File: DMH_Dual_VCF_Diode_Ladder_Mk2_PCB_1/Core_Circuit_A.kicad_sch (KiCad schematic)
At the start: 41 parts, among them SW1 SW_SPDT, SW2 SW_SPDT, SW3 SW_SPDT, U3 TL074, U5 TL074

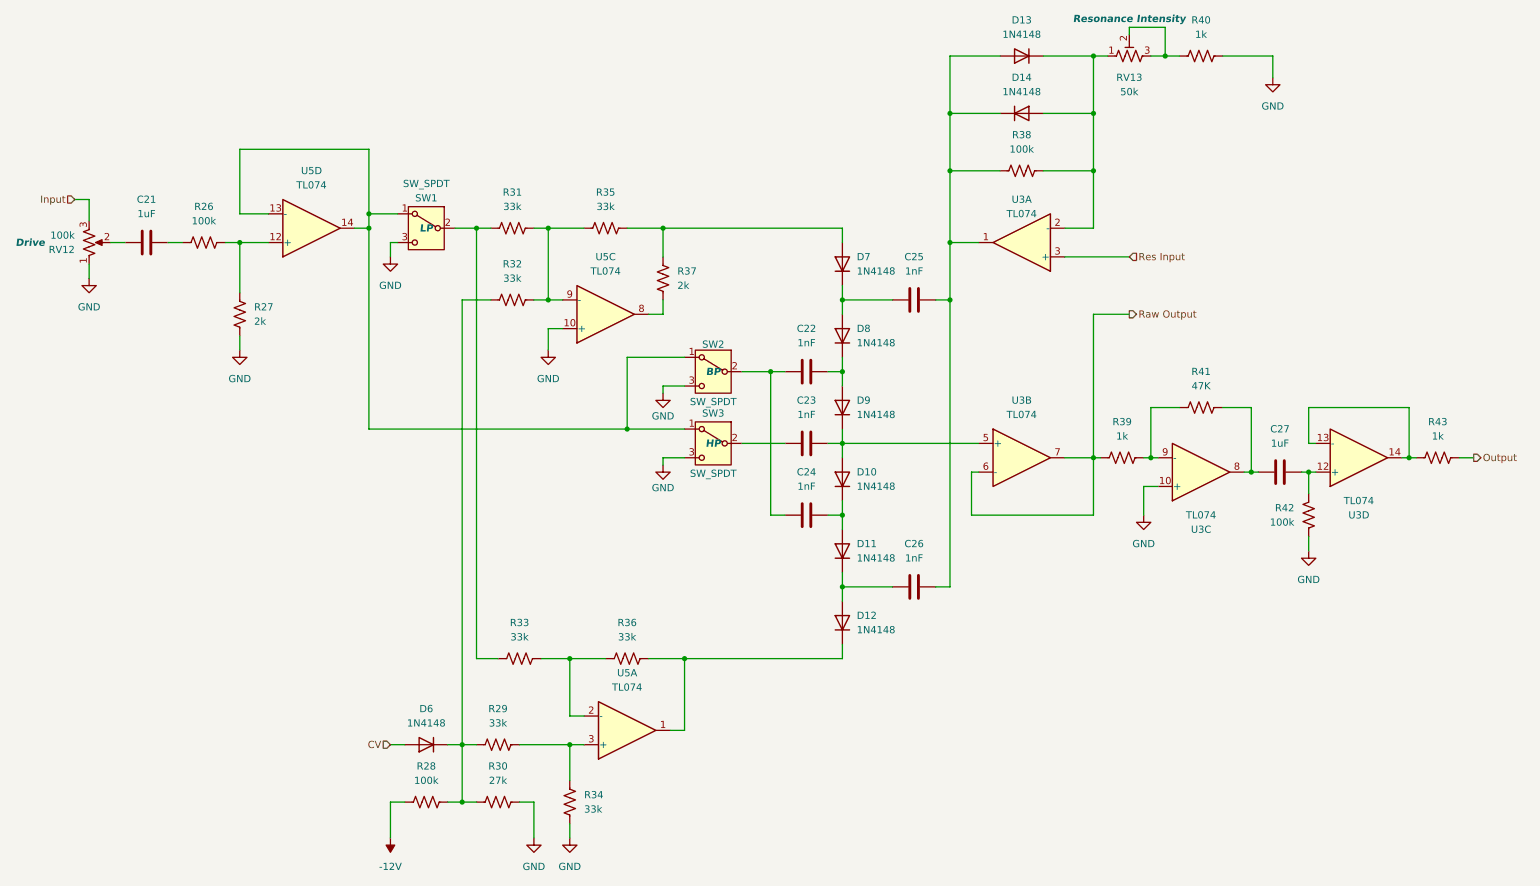
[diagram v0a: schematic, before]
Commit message: Added board-to-board pins to schematic
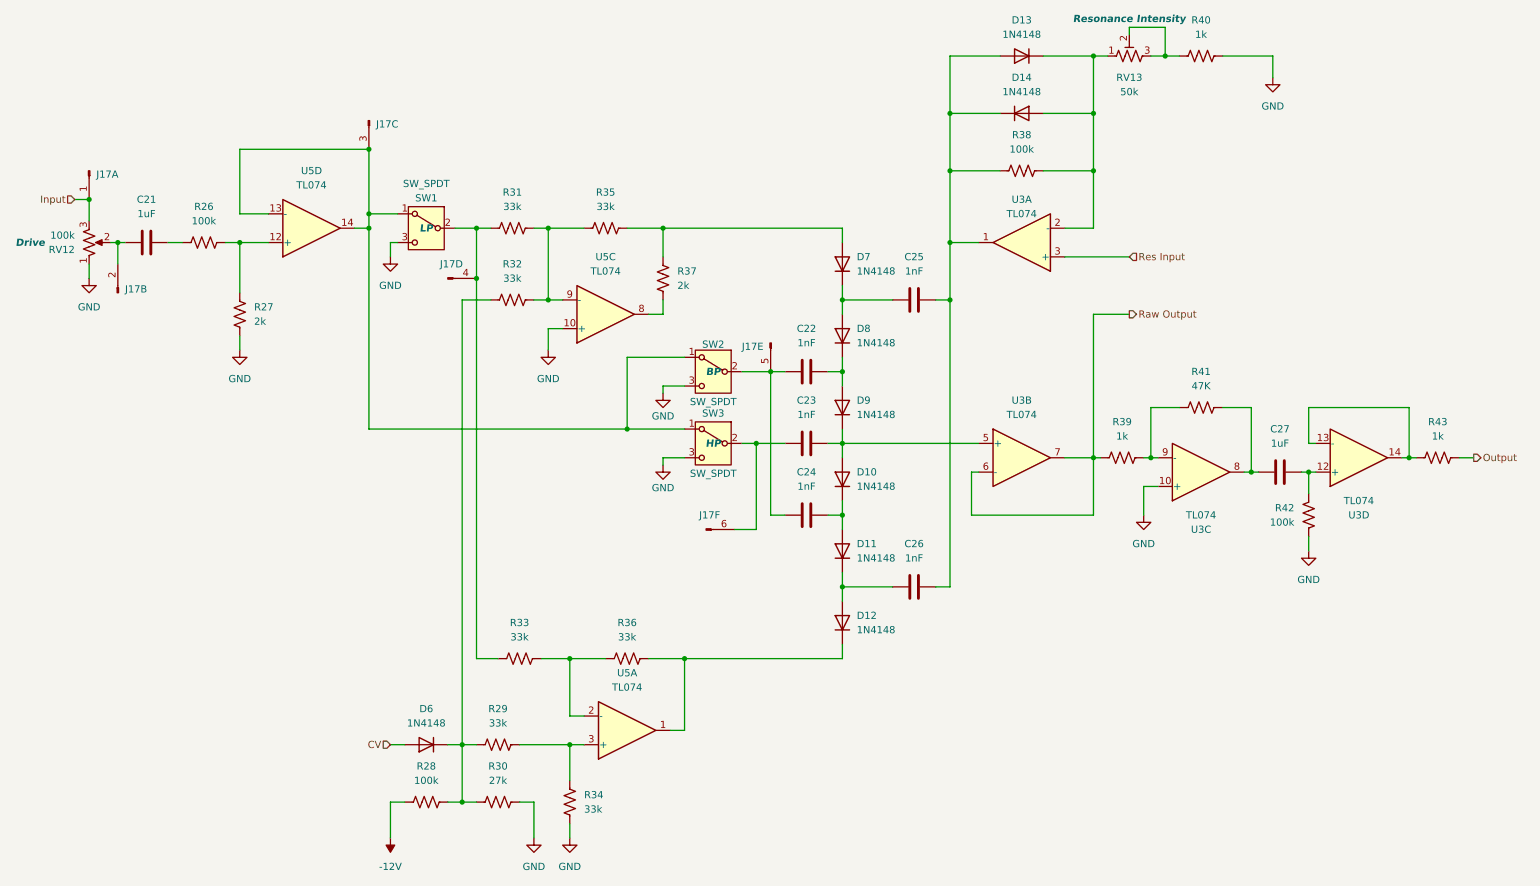
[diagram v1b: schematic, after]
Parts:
- added J17: Conn_01x10_PinHeader, Connector_PinHeader_2.54mm:PinHeader_1x10_P2.54mm_Vertical, symbol SynthStuff:Conn_01x10_PinHeader
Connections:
- net Input: now also J17.1 (Pin_1)
- net at C21.1, RV12.2: now also J17.2 (Pin_2)
- net at C22.1, C24.1, SW2.2 (B): now also J17.5 (Pin_5)
- net at SW1.1 (A), SW2.1 (A), SW3.1 (A)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: now also J17.3 (Pin_3)
- net at R31.1, R33.1, SW1.2 (B): now also J17.4 (Pin_4)
- net at C23.1, SW3.2 (B): now also J17.6 (Pin_6)

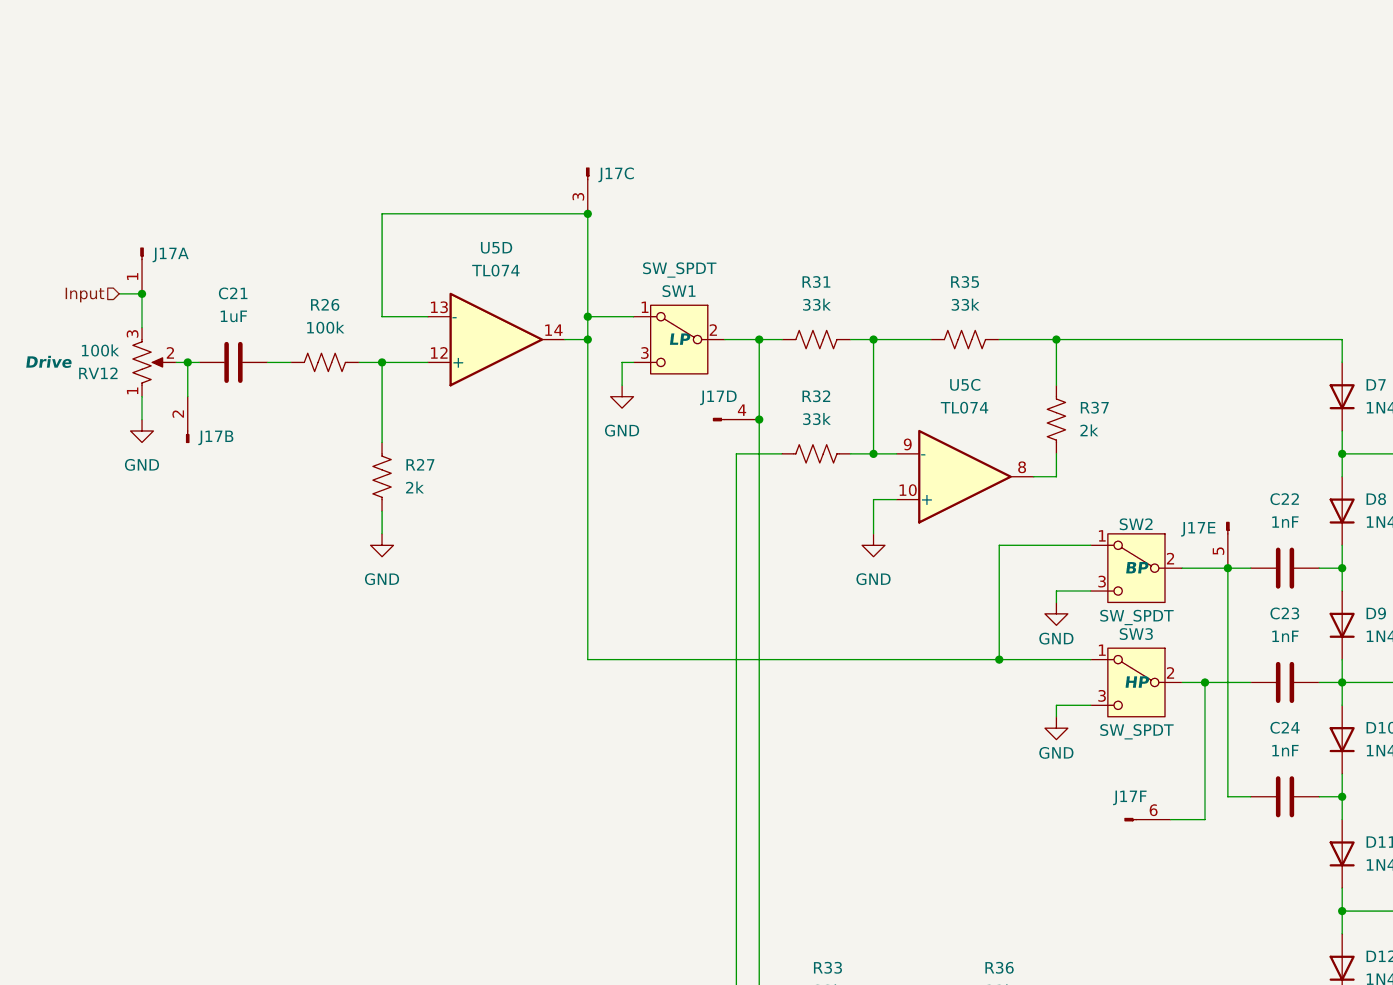
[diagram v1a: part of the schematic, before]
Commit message: Created Drive CV circuits
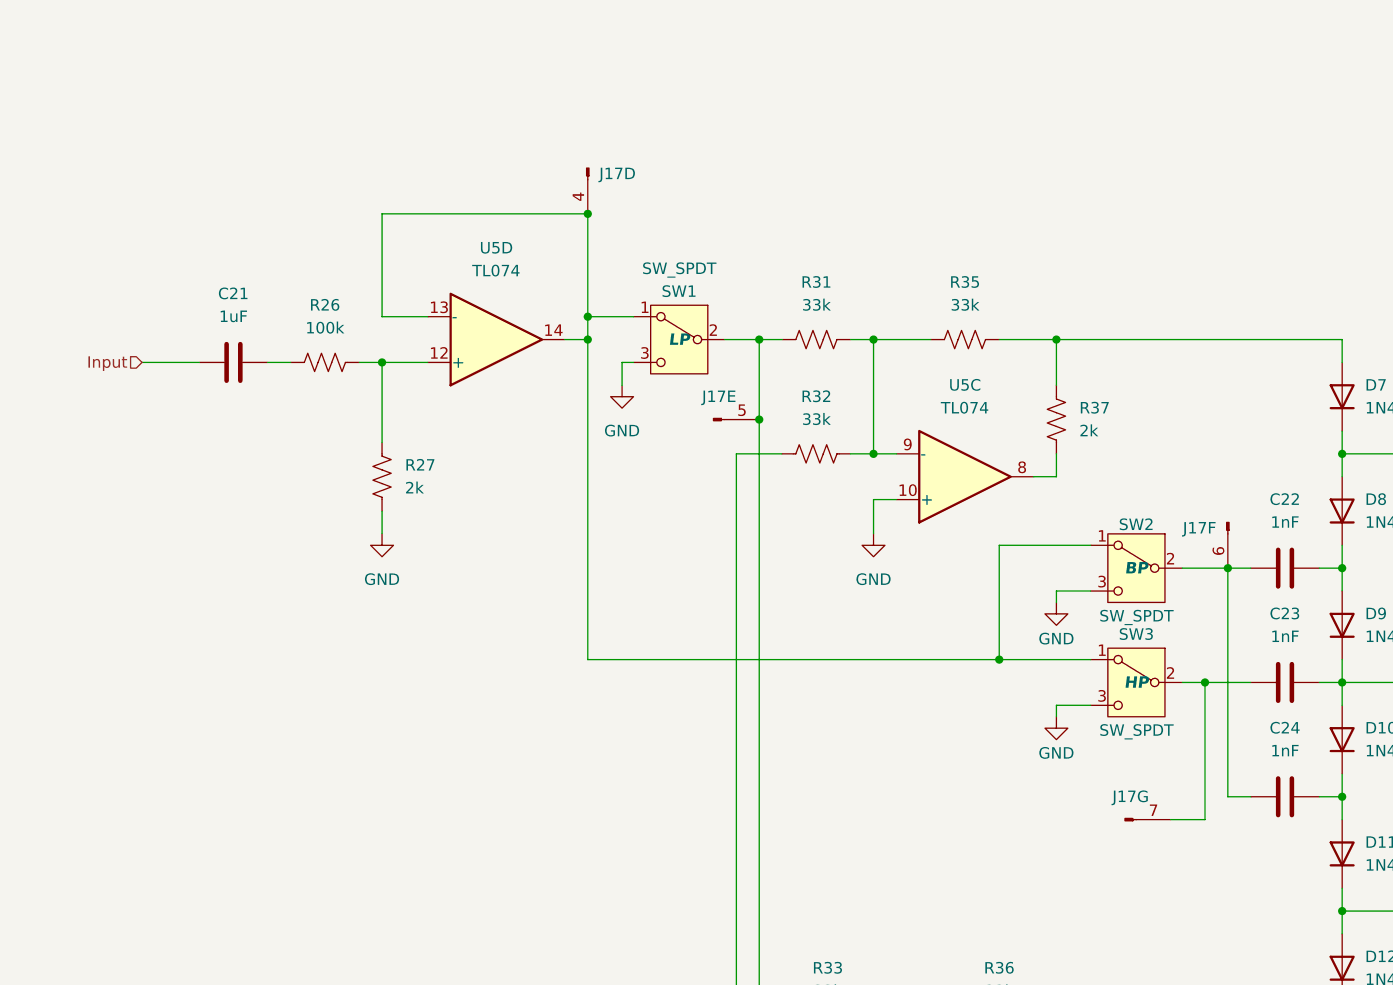
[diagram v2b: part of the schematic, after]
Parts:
- removed unit 1 of J17
- removed unit 2 of J17
- removed RV12: 100k, SynthStuff:Potentiometer_Alpha_RD901F-40-00D_Single_Vertical, symbol Device:R_Potentiometer_US
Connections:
- net Input: now also C21.1
- net at C22.1, C24.1, SW2.2 (B): now also J17.6 (Pin_6); no longer J17.5 (Pin_5)
- net at SW1.1 (A), SW2.1 (A), SW3.1 (A)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: now also J17.4 (Pin_4); no longer J17.3 (Pin_3)
- net at R31.1, R33.1, SW1.2 (B): now also J17.5 (Pin_5); no longer J17.4 (Pin_4)
- net at C23.1, SW3.2 (B): now also J17.7 (Pin_7); no longer J17.6 (Pin_6)

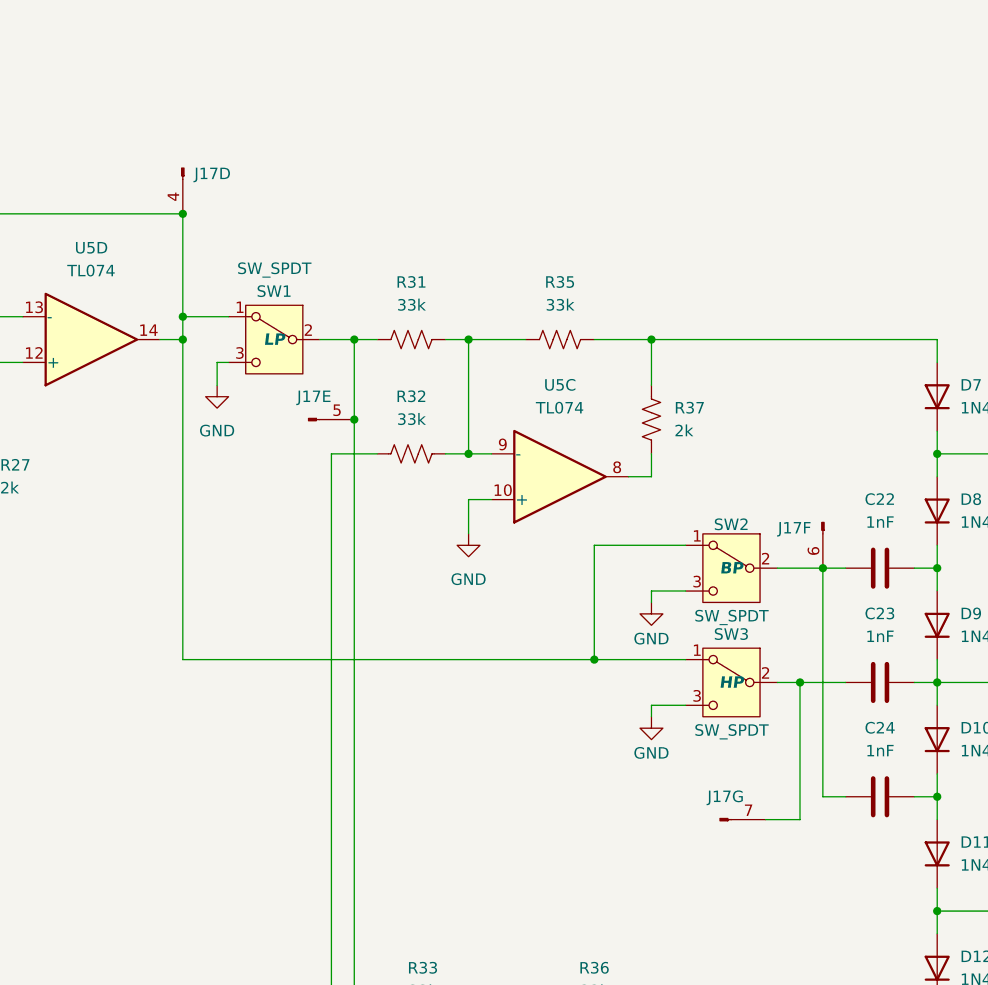
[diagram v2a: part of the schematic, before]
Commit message: Added inter-board pins to all circuits
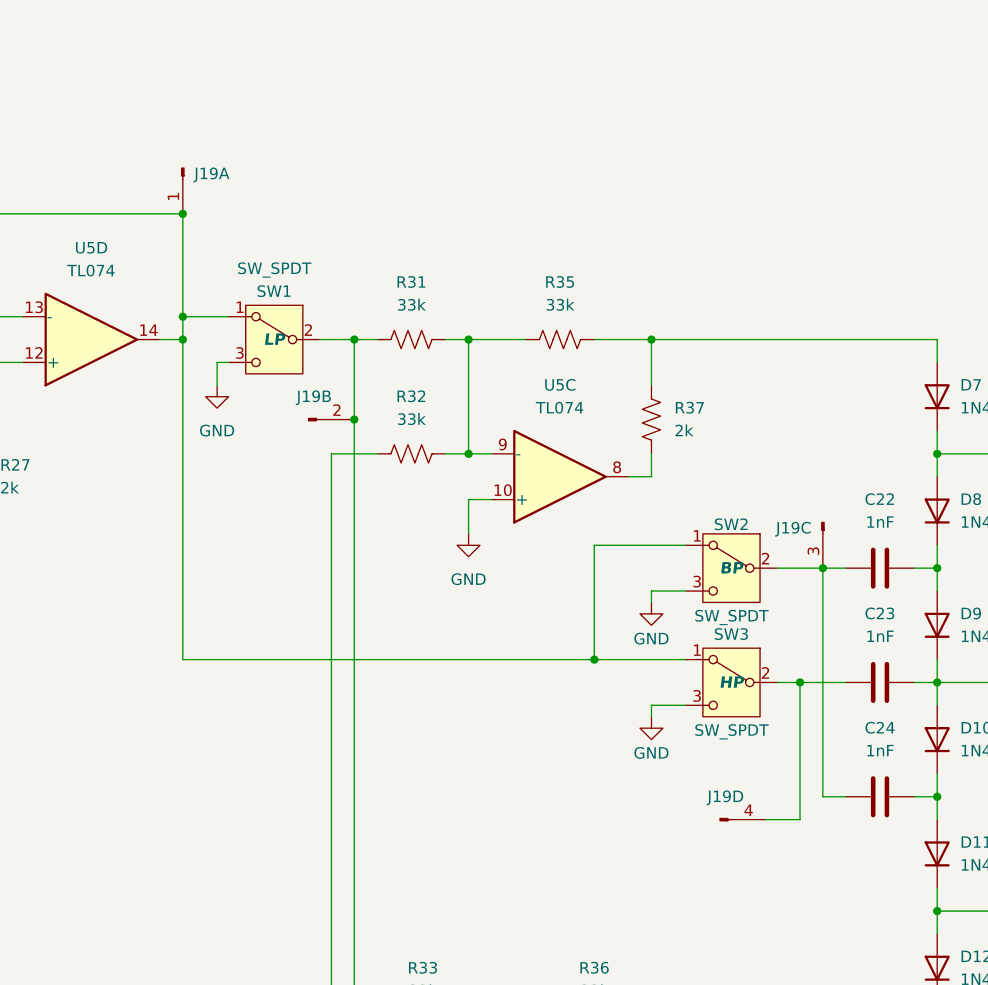
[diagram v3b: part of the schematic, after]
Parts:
- J19: renamed from J17; value Conn_01x10_PinHeader -> Conn_01x04_PinHeader; symbol SynthStuff:Conn_01x10_PinHeader -> SynthStuff:Conn_01x04_PinHeader
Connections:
- net at C22.1, C24.1, SW2.2 (B): now also J19.3 (Pin_3); no longer J19.6 (Pin_6)
- net at SW1.1 (A), SW2.1 (A), SW3.1 (A)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: now also J19.1 (Pin_1); no longer J19.4 (Pin_4)
- net at R31.1, R33.1, SW1.2 (B): now also J19.2 (Pin_2); no longer J19.5 (Pin_5)
- net at C23.1, SW3.2 (B): now also J19.4 (Pin_4); no longer J19.7 (Pin_7)
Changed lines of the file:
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@@
 		(shape input)
 		(at 78.74 152.4 180)
-		(fields_autoplaced yes)
 		(effects
 			(font
@@
 		(shape output)
 		(at 209.55 76.2 0)
-		(fields_autoplaced yes)
 		(effects
 			(font
@@
 		(shape input)
 		(at 25.4 63.5 180)
-		(fields_autoplaced yes)
 		(effects
 			(font
@@
 		(shape output)
 		(at 270.51 101.6 0)
-		(fields_autoplaced yes)
 		(effects
 			(font
@@
 		(shape input)
 		(at 209.55 66.04 0)
-		(fields_autoplaced yes)
 		(effects
 			(font
@@
 	)
 	(symbol
-		(lib_id "SynthStuff:Conn_01x10_PinHeader")
+		(lib_id "SynthStuff:Conn_01x04_PinHeader")
 		(at 146.05 81.28 270)
-		(unit 6)
+		(unit 3)
 		(exclude_from_sim no)
 		(in_bom yes)
 		(on_board yes)
 		(dnp no)
-		(property "Reference" "J17"
+		(property "Reference" "J19"
 			(at 144.78 81.9149 90)
 			(effects
@@
 			)
 		)
-		(property "Value" "Conn_01x10_PinHeader"
+		(property "Value" "Conn_01x04_PinHeader"
 			(at 143.51 81.28 0)
 			(effects
@@
 			)
 		)
-		(property "Description" "Generic connector, single row, 01x10"
+		(property "Description" "Generic connector, single row, 01x04"
 			(at 146.05 81.28 0)
 			(effects
@@
 		(pin "1"
 		)
-		(pin "7"
-		)
 		(pin "2"
 		)
-		(pin "5"
-		)
 		(pin "3"
 		)
-		(pin "10"
-		)
 		(pin "4"
 		)
-		(pin "9"
-		)
-		(pin "6"
-		)
-		(pin "8"
-		)
 		(instances
 			(project ""
 				(path "/58f4306d-5387-4983-bb08-41a2313fd315/7ad2d702-dfb7-4d49-a82d-34430dd5948f"
-					(reference "J17")
-					(unit 6)
+					(reference "J19")
+					(unit 3)
 				)
 			)
@@
 	)
 	(symbol
-		(lib_id "SynthStuff:Conn_01x10_PinHeader")
+		(lib_id "SynthStuff:Conn_01x04_PinHeader")
 		(at 74.93 41.91 270)
-		(unit 4)
+		(unit 1)
 		(exclude_from_sim no)
 		(in_bom yes)
@@
 		(dnp no)
 		(fields_autoplaced yes)
-		(property "Reference" "J17"
+		(property "Reference" "J19"
 			(at 76.2 42.5449 90)
 			(effects
@@
 			)
 		)
-		(property "Value" "Conn_01x10_PinHeader"
+		(property "Value" "Conn_01x04_PinHeader"
 			(at 72.39 41.91 0)
 			(effects
@@
 			)
 		)
-		(property "Description" "Generic connector, single row, 01x10"
+		(property "Description" "Generic connector, single row, 01x04"
 			(at 74.93 41.91 0)
 			(effects
@@
 			)
 		)
-		(pin "6"
-		)
 		(pin "3"
 		)
-		(pin "7"
-		)
 		(pin "2"
 		)
-		(pin "9"
-		)
 		(pin "4"
 		)
-		(pin "5"
-		)
-		(pin "10"
-		)
 		(pin "1"
 		)
-		(pin "8"
-		)
 		(instances
 			(project ""
 				(path "/58f4306d-5387-4983-bb08-41a2313fd315/7ad2d702-dfb7-4d49-a82d-34430dd5948f"
-					(reference "J17")
-					(unit 4)
+					(reference "J19")
+					(unit 1)
 				)
 			)
@@
 	)
 	(symbol
-		(lib_id "SynthStuff:Conn_01x10_PinHeader")
+		(lib_id "SynthStuff:Conn_01x04_PinHeader")
 		(at 134.62 114.3 0)
 		(mirror x)
-		(unit 7)
+		(unit 4)
 		(exclude_from_sim no)
 		(in_bom yes)
@@
 		(dnp no)
 		(fields_autoplaced yes)
-		(property "Reference" "J17"
+		(property "Reference" "J19"
 			(at 135.255 111.76 0)
 			(effects
@@
 			)
 		)
-		(property "Value" "Conn_01x10_PinHeader"
+		(property "Value" "Conn_01x04_PinHeader"
 			(at 134.62 111.76 0)
 			(effects
@@
 			)
 		)
-		(property "Description" "Generic connector, single row, 01x10"
+		(property "Description" "Generic connector, single row, 01x04"
 			(at 134.62 114.3 0)
 			(effects
@@
 		(pin "1"
 		)
-		(pin "7"
-		)
 		(pin "2"
 		)
-		(pin "5"
-		)
 		(pin "3"
 		)
-		(pin "10"
-		)
 		(pin "4"
 		)
-		(pin "9"
-		)
-		(pin "6"
-		)
-		(pin "8"
-		)
 		(instances
 			(project ""
 				(path "/58f4306d-5387-4983-bb08-41a2313fd315/7ad2d702-dfb7-4d49-a82d-34430dd5948f"
-					(reference "J17")
-					(unit 7)
+					(reference "J19")
+					(unit 4)
 				)
 			)
@@
 	)
 	(symbol
-		(lib_id "SynthStuff:Conn_01x10_PinHeader")
+		(lib_id "SynthStuff:Conn_01x04_PinHeader")
 		(at 88.9 69.85 0)
-		(unit 5)
+		(unit 2)
 		(exclude_from_sim no)
 		(in_bom yes)
@@
 		(dnp no)
 		(fields_autoplaced yes)
-		(property "Reference" "J17"
+		(property "Reference" "J19"
 			(at 89.535 67.31 0)
 			(effects
@@
 			)
 		)
-		(property "Value" "Conn_01x10_PinHeader"
+		(property "Value" "Conn_01x04_PinHeader"
 			(at 88.9 72.39 0)
 			(effects
@@
 			)
 		)
-		(property "Description" "Generic connector, single row, 01x10"
+		(property "Description" "Generic connector, single row, 01x04"
 			(at 88.9 69.85 0)
 			(effects
@@
 			)
 		)
-		(pin "6"
-		)
 		(pin "3"
 		)
-		(pin "7"
-		)
 		(pin "2"
 		)
-		(pin "9"
-		)
 		(pin "4"
 		)
-		(pin "5"
-		)
-		(pin "10"
-		)
 		(pin "1"
 		)
-		(pin "8"
-		)
 		(instances
 			(project ""
 				(path "/58f4306d-5387-4983-bb08-41a2313fd315/7ad2d702-dfb7-4d49-a82d-34430dd5948f"
-					(reference "J17")
-					(unit 5)
+					(reference "J19")
+					(unit 2)
 				)
 			)
